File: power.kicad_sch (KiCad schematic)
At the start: 15 parts

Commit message: added some notes and PDF
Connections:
- net +24V: now also C5.1, U1.2 (EN), U1.3 (VIN)
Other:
- note added: "TODO: figure out how to switch between 24v rail and 5v rail for 3.3v buck supply"
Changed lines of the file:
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@@
   (junction (at 86.36 71.12) (diameter 0) (color 0 0 0 0)
+  )
+  (junction (at 79.375 71.12) (diameter 0) (color 0 0 0 0)
   )
   (junction (at 127.635 86.36) (diameter 0) (color 0 0 0 0)
@@
     (stroke (width 0) (type default))
   )
+  (wire (pts (xy 77.47 71.12) (xy 79.375 71.12))
+    (stroke (width 0) (type default))
+  )
   (wire (pts (xy 85.09 125.73) (xy 85.09 127))
+    (stroke (width 0) (type default))
+  )
+  (wire (pts (xy 77.47 69.85) (xy 77.47 71.12))
     (stroke (width 0) (type default))
   )
@@
     (effects (font (size 1.27 1.27)) (justify left bottom))
   )
+  (text "TODO:\nfigure out how to switch\nbetween 24v rail and 5v \nrail for 3.3v buck supply"
+    (at 63.5 61.595 0)
+    (effects (font (size 1.27 1.27)) (justify left bottom))
+  )

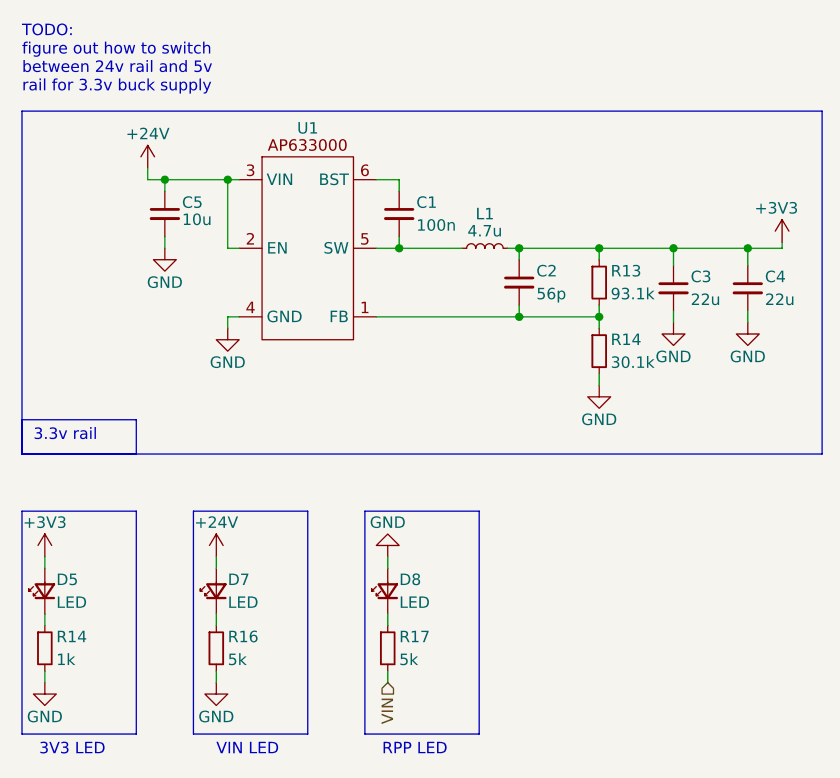
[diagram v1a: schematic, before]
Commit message: started on layout and added SD/flash/BNO
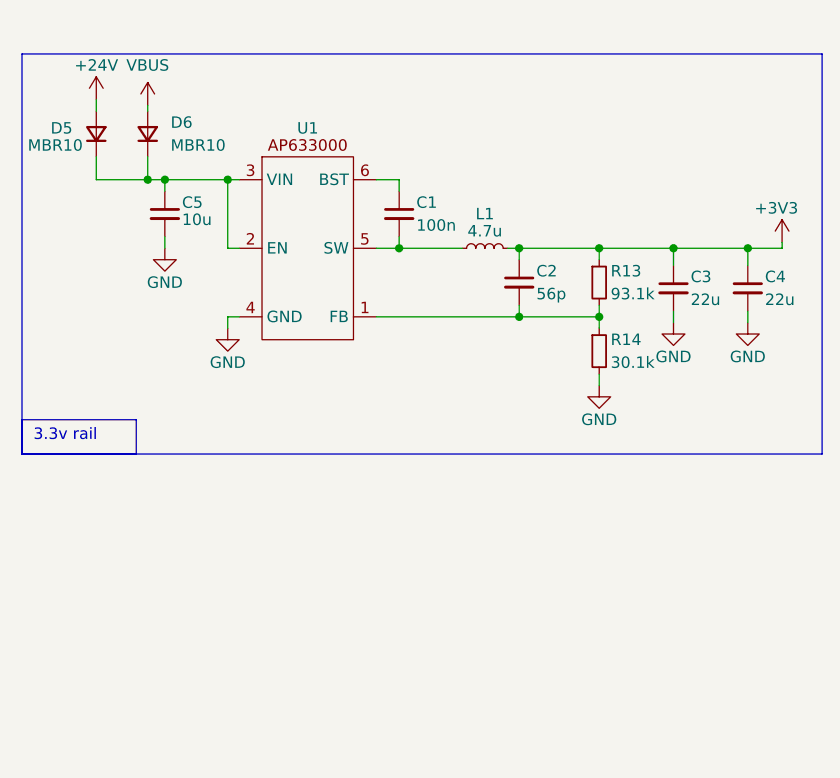
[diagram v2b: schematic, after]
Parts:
- removed D5, D7, D8: LED, LED_SMD:LED_0603_1608Metric, symbol Device:LED_Small
- removed R14: 1k, Resistor_SMD:R_0603_1608Metric, symbol Device:R_Small
- removed R16, R17: 5k, Resistor_SMD:R_0603_1608Metric, symbol Device:R_Small
- added D5, D6: MBR10, TO-227:TO-277-D, symbol Device:D_Small
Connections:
- net +24V: now also D5.2 (A); no longer C5.1, U1.2 (EN), U1.3 (VIN)
- new net: C5.1, D5.1 (K), D6.1 (K), U1.2 (EN), U1.3 (VIN)
- new net VBUS: D6.2 (A)
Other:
- note removed: "3V3 LED"
- note removed: "RPP LED"
- note removed: "TODO: figure out how to switch between 24v rail and 5v rail for 3.3v buck supply"
- note removed: "VIN LED"

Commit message: final
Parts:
- renumbered D5 to D2, D6 to D3
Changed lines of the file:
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@@
     (pin "1")
     (instances
-      (project "UMRT_FC_R1"
+      (project "UMRT_FC_R2"
         (path "/27c40824-3c02-48dc-87e8-ac576671a38f"
           (reference "#PWR09") (unit 1)
@@
         )
         (path "/27c40824-3c02-48dc-87e8-ac576671a38f/a58a71ea-f1fa-4532-9300-f7482fcf2a19"
-          (reference "#PWR053") (unit 1)
+          (reference "#PWR052") (unit 1)
         )
       )
@@
     (pin "1")
     (instances
-      (project "UMRT_FC_R1"
+      (project "UMRT_FC_R2"
         (path "/27c40824-3c02-48dc-87e8-ac576671a38f"
           (reference "#PWR010") (unit 1)
@@
         )
         (path "/27c40824-3c02-48dc-87e8-ac576671a38f/a58a71ea-f1fa-4532-9300-f7482fcf2a19"
-          (reference "#PWR052") (unit 1)
+          (reference "#PWR051") (unit 1)
         )
       )
@@
     (pin "6")
     (instances
-      (project "UMRT_FC_R1"
+      (project "UMRT_FC_R2"
         (path "/27c40824-3c02-48dc-87e8-ac576671a38f"
           (reference "U1") (unit 1)
@@
         )
         (path "/27c40824-3c02-48dc-87e8-ac576671a38f/a58a71ea-f1fa-4532-9300-f7482fcf2a19"
-          (reference "U10") (unit 1)
+          (reference "U6") (unit 1)
         )
       )
@@
     (pin "1")
     (instances
-      (project "UMRT_FC_R1"
+      (project "UMRT_FC_R2"
         (path "/27c40824-3c02-48dc-87e8-ac576671a38f"
           (reference "#PWR013") (unit 1)
@@
         )
         (path "/27c40824-3c02-48dc-87e8-ac576671a38f/a58a71ea-f1fa-4532-9300-f7482fcf2a19"
-          (reference "#PWR051") (unit 1)
+          (reference "#PWR050") (unit 1)
         )
       )
@@
   (symbol (lib_id "Device:D_Small") (at 71.755 66.04 90) (unit 1)
     (in_bom yes) (on_board yes) (dnp no)
-    (property "Reference" "D5" (at 66.675 65.405 90)
+    (property "Reference" "D2" (at 66.675 65.405 90)
       (effects (font (size 1.27 1.27)) (justify right))
     )
@@
     (pin "2")
     (instances
-      (project "UMRT_FC_R1"
-        (path "/27c40824-3c02-48dc-87e8-ac576671a38f/a58a71ea-f1fa-4532-9300-f7482fcf2a19"
-          (reference "D5") (unit 1)
+      (project "UMRT_FC_R2"
+        (path "/27c40824-3c02-48dc-87e8-ac576671a38f/a58a71ea-f1fa-4532-9300-f7482fcf2a19"
+          (reference "D2") (unit 1)
         )
       )
@@
   (symbol (lib_id "power:+3V3") (at 147.955 78.105 0) (unit 1)
     (in_bom yes) (on_board yes) (dnp no)
-    (property "Reference" "#PWR056" (at 147.955 81.915 0)
+    (property "Reference" "#PWR055" (at 147.955 81.915 0)
       (effects (font (size 1.27 1.27)) hide)
     )
@@
     (pin "1")
     (instances
-      (project "UMRT_FC_R1"
-        (path "/27c40824-3c02-48dc-87e8-ac576671a38f/a58a71ea-f1fa-4532-9300-f7482fcf2a19"
-          (reference "#PWR056") (unit 1)
+      (project "UMRT_FC_R2"
+        (path "/27c40824-3c02-48dc-87e8-ac576671a38f/a58a71ea-f1fa-4532-9300-f7482fcf2a19"
+          (reference "#PWR055") (unit 1)
         )
       )
@@
   (symbol (lib_id "power:VBUS") (at 77.47 62.865 0) (unit 1)
     (in_bom yes) (on_board yes) (dnp no) (fields_autoplaced)
-    (property "Reference" "#PWR050" (at 77.47 66.675 0)
+    (property "Reference" "#PWR049" (at 77.47 66.675 0)
       (effects (font (size 1.27 1.27)) hide)
     )
@@
     (pin "1")
     (instances
-      (project "UMRT_FC_R1"
-        (path "/27c40824-3c02-48dc-87e8-ac576671a38f/a58a71ea-f1fa-4532-9300-f7482fcf2a19"
-          (reference "#PWR050") (unit 1)
+      (project "UMRT_FC_R2"
+        (path "/27c40824-3c02-48dc-87e8-ac576671a38f/a58a71ea-f1fa-4532-9300-f7482fcf2a19"
+          (reference "#PWR049") (unit 1)
         )
       )
@@
     (pin "2")
     (instances
-      (project "UMRT_FC_R1"
+      (project "UMRT_FC_R2"
         (path "/27c40824-3c02-48dc-87e8-ac576671a38f"
           (reference "C2") (unit 1)
@@
         )
         (path "/27c40824-3c02-48dc-87e8-ac576671a38f/a58a71ea-f1fa-4532-9300-f7482fcf2a19"
-          (reference "C35") (unit 1)
+          (reference "C28") (unit 1)
         )
       )
@@
     (pin "1")
     (instances
-      (project "UMRT_FC_R1"
+      (project "UMRT_FC_R2"
         (path "/27c40824-3c02-48dc-87e8-ac576671a38f/49f25279-4955-4ac4-b0d8-280c183177c3"
           (reference "#PWR02") (unit 1)
         )
         (path "/27c40824-3c02-48dc-87e8-ac576671a38f/a58a71ea-f1fa-4532-9300-f7482fcf2a19"
-          (reference "#PWR049") (unit 1)
+          (reference "#PWR048") (unit 1)
         )
       )
@@
     (pin "2")
     (instances
-      (project "UMRT_FC_R1"
+      (project "UMRT_FC_R2"
         (path "/27c40824-3c02-48dc-87e8-ac576671a38f"
           (reference "L1") (unit 1)
@@
     (pin "2")
     (instances
-      (project "UMRT_FC_R1"
+      (project "UMRT_FC_R2"
         (path "/27c40824-3c02-48dc-87e8-ac576671a38f"
           (reference "R13") (unit 1)
@@
         )
         (path "/27c40824-3c02-48dc-87e8-ac576671a38f/a58a71ea-f1fa-4532-9300-f7482fcf2a19"
-          (reference "R20") (unit 1)
+          (reference "R17") (unit 1)
         )
       )
@@
     (pin "1")
     (instances
-      (project "UMRT_FC_R1"
+      (project "UMRT_FC_R2"
         (path "/27c40824-3c02-48dc-87e8-ac576671a38f"
           (reference "#PWR011") (unit 1)
@@
         )
         (path "/27c40824-3c02-48dc-87e8-ac576671a38f/a58a71ea-f1fa-4532-9300-f7482fcf2a19"
-          (reference "#PWR054") (unit 1)
+          (reference "#PWR053") (unit 1)
         )
       )
@@
     (pin "2")
     (instances
-      (project "UMRT_FC_R1"
+      (project "UMRT_FC_R2"
         (path "/27c40824-3c02-48dc-87e8-ac576671a38f"
           (reference "C5") (unit 1)
@@
         )
         (path "/27c40824-3c02-48dc-87e8-ac576671a38f/a58a71ea-f1fa-4532-9300-f7482fcf2a19"
-          (reference "C33") (unit 1)
+          (reference "C26") (unit 1)
         )
       )
@@
   (symbol (lib_id "Device:D_Small") (at 77.47 66.04 90) (unit 1)
     (in_bom yes) (on_board yes) (dnp no) (fields_autoplaced)
-    (property "Reference" "D6" (at 80.01 64.77 90)
+    (property "Reference" "D3" (at 80.01 64.77 90)
       (effects (font (size 1.27 1.27)) (justify right))
     )
@@
     (pin "2")
     (instances
-      (project "UMRT_FC_R1"
-        (path "/27c40824-3c02-48dc-87e8-ac576671a38f/a58a71ea-f1fa-4532-9300-f7482fcf2a19"
-          (reference "D6") (unit 1)
+      (project "UMRT_FC_R2"
+        (path "/27c40824-3c02-48dc-87e8-ac576671a38f/a58a71ea-f1fa-4532-9300-f7482fcf2a19"
+          (reference "D3") (unit 1)
         )
       )
@@
     (pin "1")
     (instances
-      (project "UMRT_FC_R1"
+      (project "UMRT_FC_R2"
         (path "/27c40824-3c02-48dc-87e8-ac576671a38f"
           (reference "#PWR012") (unit 1)
@@
         )
         (path "/27c40824-3c02-48dc-87e8-ac576671a38f/a58a71ea-f1fa-4532-9300-f7482fcf2a19"
-          (reference "#PWR055") (unit 1)
+          (reference "#PWR054") (unit 1)
         )
       )
@@
     (pin "2")
     (instances
-      (project "UMRT_FC_R1"
+      (project "UMRT_FC_R2"
         (path "/27c40824-3c02-48dc-87e8-ac576671a38f"
           (reference "R14") (unit 1)
@@
         )
         (path "/27c40824-3c02-48dc-87e8-ac576671a38f/a58a71ea-f1fa-4532-9300-f7482fcf2a19"
-          (reference "R21") (unit 1)
+          (reference "R18") (unit 1)
         )
       )
@@
     (pin "2")
     (instances
-      (project "UMRT_FC_R1"
+      (project "UMRT_FC_R2"
         (path "/27c40824-3c02-48dc-87e8-ac576671a38f"
           (reference "C1") (unit 1)
@@
         )
         (path "/27c40824-3c02-48dc-87e8-ac576671a38f/a58a71ea-f1fa-4532-9300-f7482fcf2a19"
-          (reference "C34") (unit 1)
+          (reference "C27") (unit 1)
         )
       )
@@
     (pin "2")
     (instances
-      (project "UMRT_FC_R1"
+      (project "UMRT_FC_R2"
         (path "/27c40824-3c02-48dc-87e8-ac576671a38f"
           (reference "C4") (unit 1)
@@
         )
         (path "/27c40824-3c02-48dc-87e8-ac576671a38f/a58a71ea-f1fa-4532-9300-f7482fcf2a19"
-          (reference "C37") (unit 1)
+          (reference "C30") (unit 1)
         )
       )
@@
     (pin "2")
     (instances
-      (project "UMRT_FC_R1"
+      (project "UMRT_FC_R2"
         (path "/27c40824-3c02-48dc-87e8-ac576671a38f"
           (reference "C3") (unit 1)
@@
         )
         (path "/27c40824-3c02-48dc-87e8-ac576671a38f/a58a71ea-f1fa-4532-9300-f7482fcf2a19"
-          (reference "C36") (unit 1)
-        )
-      )
+          (reference "C29") (unit 1)
+        )
+      )
